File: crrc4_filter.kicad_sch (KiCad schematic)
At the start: 0 parts

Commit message: Started on schematic, added rc_filter_stage.kicad_sch
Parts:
- added C1, C2: C, symbol Device:C
- added C3: 50p, symbol Device:C
- added J1, J2: Conn_Coaxial, symbol Connector:Conn_Coaxial
- added R1, R4: 50R, symbol Device:R_US
- added R2, R3, R5: 100K, symbol Device:R_US
- added R6: 2K, symbol Device:R_US
- added R?: 50, symbol Device:R_US
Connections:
- new net: C1.1, J1.1 (In), R3.1
- new net: C2.2, J2.1 (In), R5.1
- new net: C2.1, R1.2, R2.1
- new net: C3.1, R?.2
- new net GND: J1.2 (Ext), J2.2 (Ext), R2.2, R3.2, R4.2, R5.2, R6.2
- new net from_block_in: C1.2, R4.1
- new net from_cr: C3.2, R6.1
- new net to_block_out: R1.1
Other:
- added sheet RC Filter Stage1 (rc_filter_stage.kicad_sch)
- added sheet RC Filter Stage2 (rc_filter_stage.kicad_sch)
- added sheet RC Filter Stage3 (rc_filter_stage.kicad_sch)
- added sheet RC Filter Stage4 (rc_filter_stage.kicad_sch)
- note added: "100 ns integrator time constant 100 ns differentiator time constant AC coupled in/out SMA in/out connectors +/- 5 V DC power?"
- note added: "CR Filter"
- note added: "buffer"

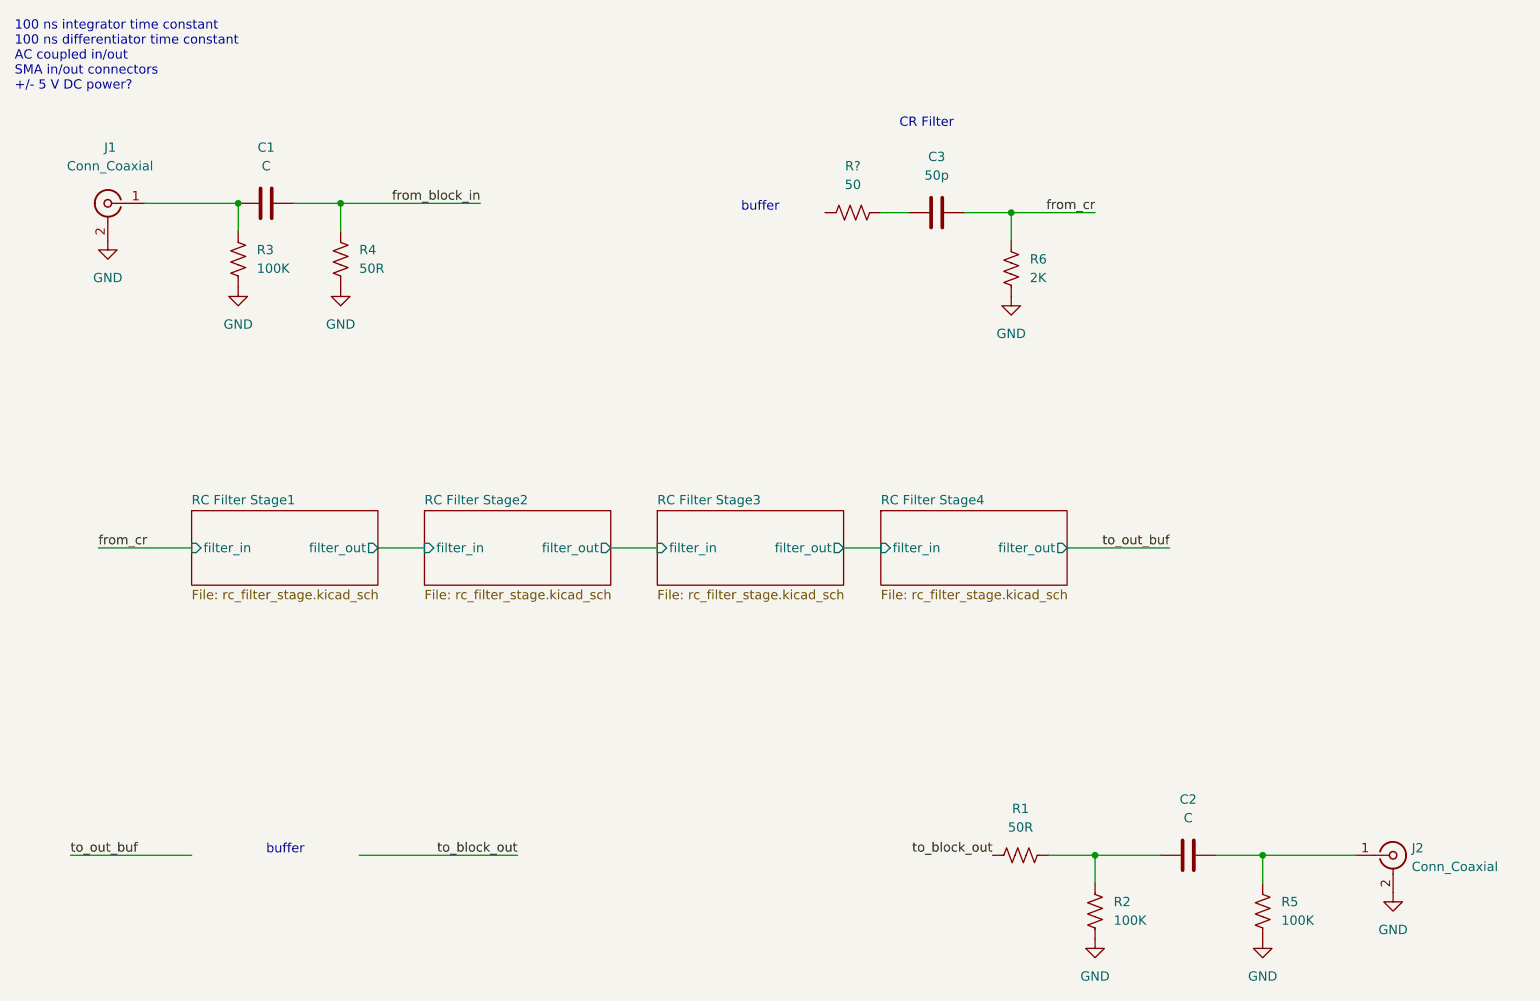
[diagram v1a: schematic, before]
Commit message: Added amplifier to rc filter
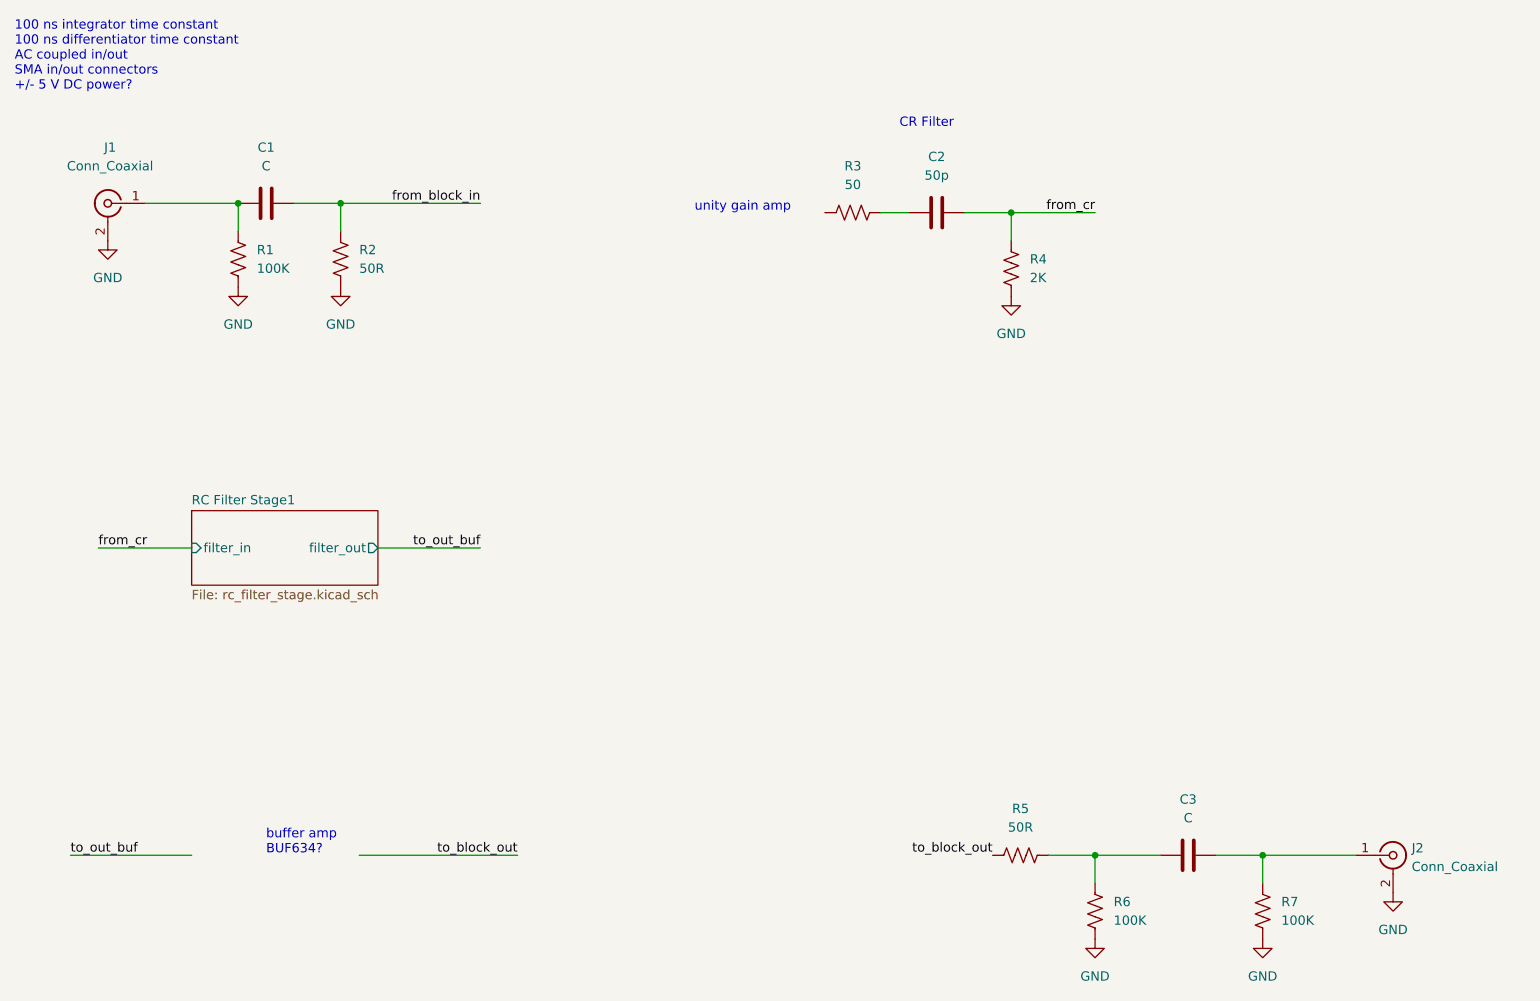
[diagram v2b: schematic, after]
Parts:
- gave numbers to parts that had none: 1
- renumbered C3 to C2, C2 to C3, R3 to R1, R4 to R2, R6 to R4, R1 to R5, R2 to R6, R5 to R7
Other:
- removed sheet RC Filter Stage2
- removed sheet RC Filter Stage3
- removed sheet RC Filter Stage4
- note added: "buffer amp BUF634?"
- note added: "unity gain amp"
- note removed: "buffer"
